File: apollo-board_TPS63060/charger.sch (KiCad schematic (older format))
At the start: 27 parts, among them J4 DNP/JST_ZH_S2B_thru, J5 DNP/JST_XH_S2B_thru, Q12 DMP2035UVT, Q15 DMN3023L, Q3 DMN3023L, Q4 2N7002A, U4 LTC4162EUFD-LAD

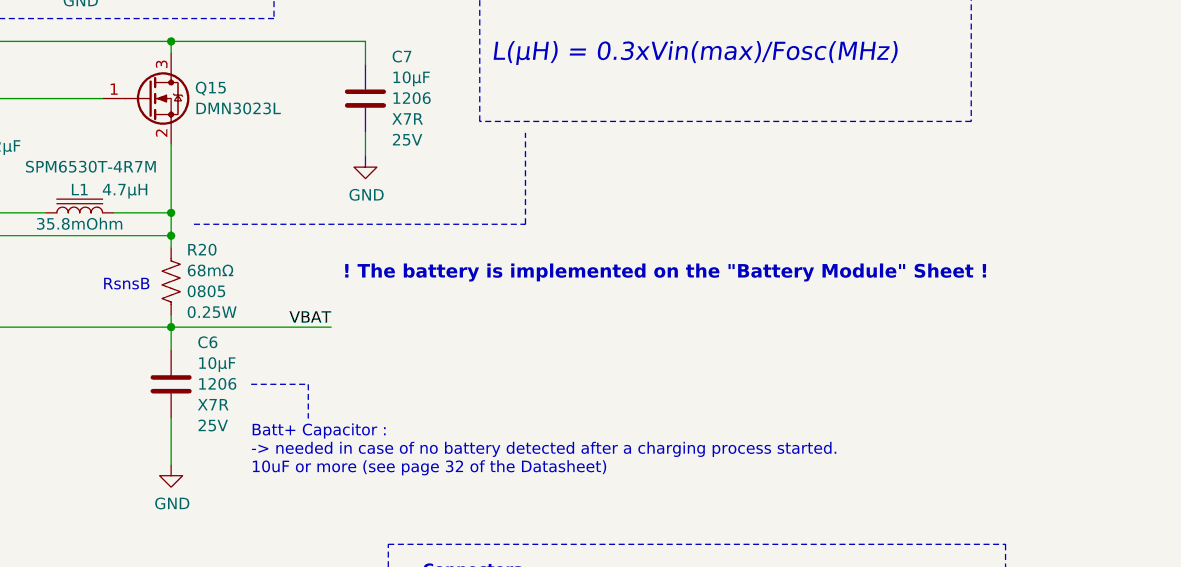
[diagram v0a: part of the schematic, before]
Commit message: Add second 0805 resistor for Rsns (R20)
- Add second 0805 resistor for Rsns (R20) and update values by 130 mOhm
- Update Silkscreen layer (Ref Des. , text, etc.)
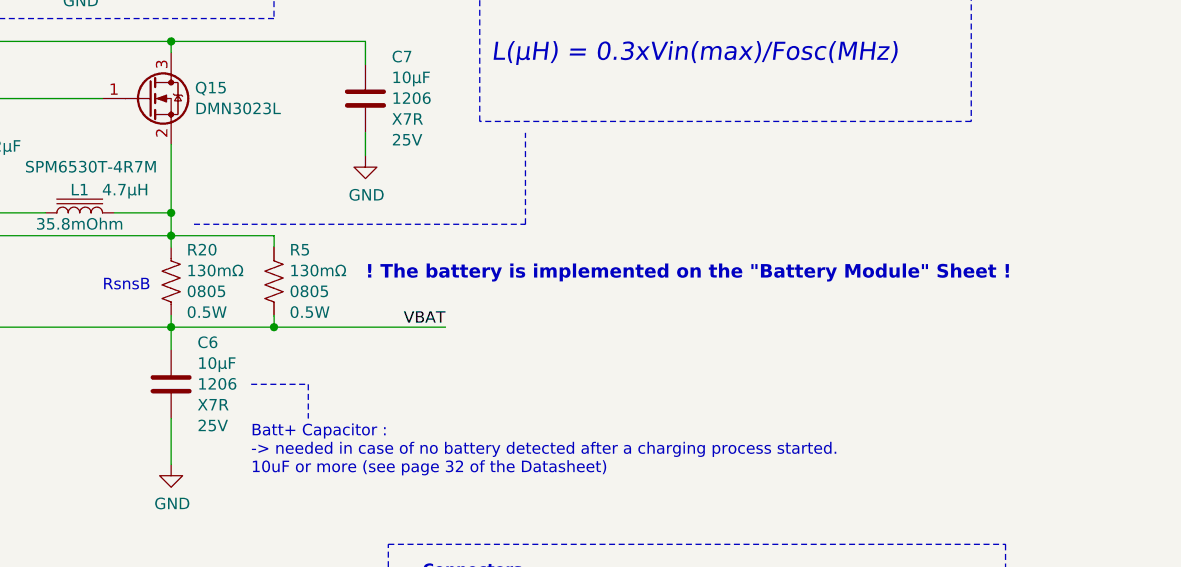
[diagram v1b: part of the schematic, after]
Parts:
- removed R20: RL0805FR-7W0R068L, Resistor_SMD:R_0805_2012Metric, symbol rl0805fr-7w0r068l:RL0805FR-7W0R068L
- added R20, R5: ERJ-6DSFR13V, Resistor_SMD:R_0805_2012Metric, symbol erj-6dsfr13v:ERJ-6DSFR13V
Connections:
- net CSP: now also R20.1, R5.1
- net VBAT: now also R20.2, R5.2

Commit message: Update 0805 resistor library link issue
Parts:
- R20, R5: symbol erj-6dsfr13v:ERJ-6DSFR13V -> ERJ-6DSFR13V:ERJ-6DSFR13V
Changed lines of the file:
@@
 BATFET
 $Comp
-L erj-6dsfr13v:ERJ-6DSFR13V R20
+L ERJ-6DSFR13V:ERJ-6DSFR13V R20
 U 1 1 610916CE
 P 7450 4150
@@
 $EndComp
 $Comp
-L erj-6dsfr13v:ERJ-6DSFR13V R5
+L ERJ-6DSFR13V:ERJ-6DSFR13V R5
 U 1 1 61093977
 P 7900 4150

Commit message: Update LED2 value as DNP + Manually Update BOM
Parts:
- LED2: value 150060YS75000_0603 -> DNP/150060YS75000_0603
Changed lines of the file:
@@
 P 2150 3750
 F 0 "LED2" H 2143 3405 50  0000 C CNN
-F 1 "150060YS75000_0603" H 2150 3650 50  0001 C CNN
+F 1 "DNP/150060YS75000_0603" H 2150 3650 50  0001 C CNN
 F 2 "LED_SMD:LED_0603_1608Metric" H 2150 3750 50  0001 C CNN
 F 3 "https://www.we-online.com/catalog/datasheet/150060YS75000.pdf" H 2150 3750 50  0001 C CNN
